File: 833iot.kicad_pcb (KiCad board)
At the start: 2 copper layers, 26.5 x 42 mm, 24 parts, among them J1 U254-051T-4BH83-F1S, J2 Conn_01x04, J3 Conn_01x02, J4 Conn_01x15_Male, J5 Conn_01x15_Male, Q1 AO3407, Q2 AO3407, SW1 SW_SPST, U1 E73-2G4M08S1E, U2 AP2112K-3.3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

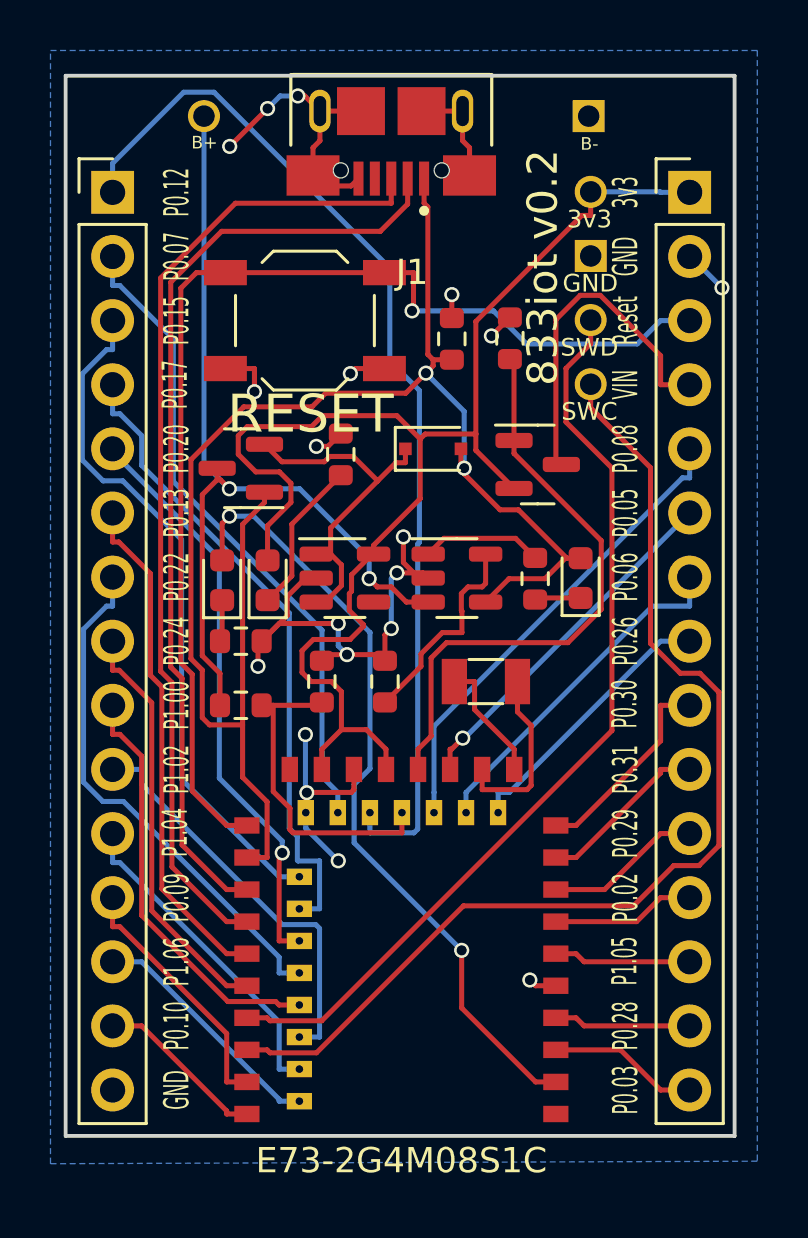
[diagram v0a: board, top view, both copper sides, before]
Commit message: fix vias issue
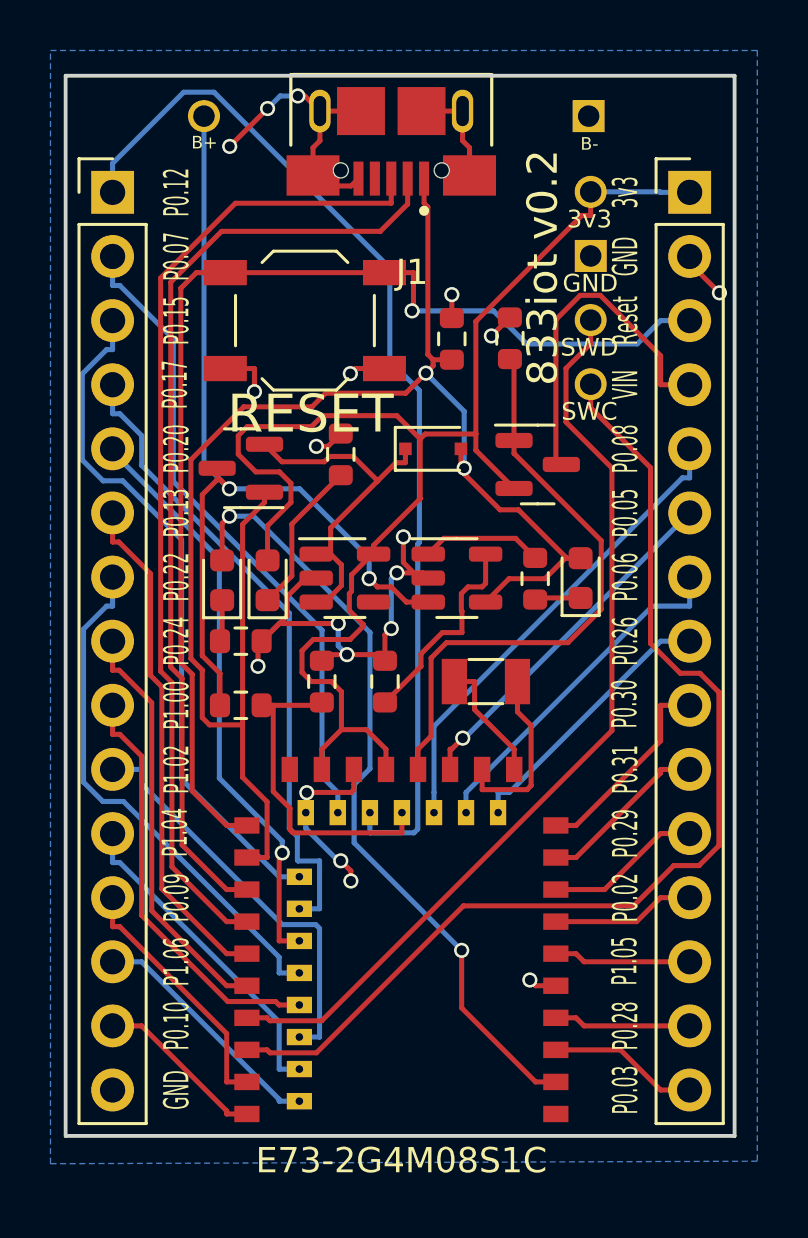
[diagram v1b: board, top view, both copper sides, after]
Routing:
- net GND: track 53.6 -> 52.5 mm
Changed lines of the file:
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@@
   (segment (start 28.4025 23.0028) (end 29.6528 23.0028) (width 0.2) (layer "F.Cu") (net 2))
   (segment (start 24.6953 36.285) (end 25.2025 35.7778) (width 0.2) (layer "F.Cu") (net 2))
+  (segment (start 39.0225 28.7628) (end 39.0225 29.022742) (width 0.2) (layer "F.Cu") (net 2))
   (segment (start 22.767525 43.302775) (end 25.102533 43.302775) (width 0.2) (layer "F.Cu") (net 2))
   (segment (start 24.1025 25.5528) (end 24.1025 24.4525) (width 0.2) (layer "F.Cu") (net 2))
@@
   (segment (start 23.0787 42.9916) (end 23.0787 42.2345) (width 0.2) (layer "F.Cu") (net 2))
   (segment (start 23.0787 42.2345) (end 23.8104 41.5028) (width 0.2) (layer "F.Cu") (net 2))
+  (segment (start 25.602533 53.102775) (end 25.202533 52.702775) (width 0.2) (layer "F.Cu") (net 2))
   (segment (start 25.6121 49.9945) (end 25.7225 49.8841) (width 0.2) (layer "F.Cu") (net 2))
   (segment (start 27.426013 41.29753) (end 28.45973 41.29753) (width 0.2) (layer "F.Cu") (net 2))
   (segment (start 22.0675 44.0028) (end 22.767525 43.302775) (width 0.2) (layer "F.Cu") (net 2))
+  (segment (start 25.602533 53.502775) (end 25.602533 53.102775) (width 0.2) (layer "F.Cu") (net 2))
   (segment (start 23.8155 50.7948) (end 23.8155 49.9945) (width 0.2) (layer "F.Cu") (net 2))
   (segment (start 28.2988 41.5028) (end 28.665 41.5028) (width 0.2) (layer "F.Cu") (net 2))
@@
   (segment (start 24.3775 24.1775) (end 24.1025 24.4525) (width 0.2) (layer "F.Cu") (net 2))
   (segment (start 26.9525 44.7778) (end 26.9525 43.752808) (width 0.2) (layer "F.Cu") (net 2))
+  (segment (start 39.0225 29.022742) (end 40.202533 30.202775) (width 0.2) (layer "F.Cu") (net 2))
   (segment (start 33.7215 57.6528) (end 32.9212 57.6528) (width 0.2) (layer "F.Cu") (net 2))
   (segment (start 26.0025 23.0028) (end 24.7522 23.0028) (width 0.2) (layer "F.Cu") (net 2))
@@
   (via (at 25.102533 43.302775) (size 0.6) (drill 0.4) (layers "F.Cu" "B.Cu") (net 2))
   (via (at 21.9229 44.9964) (size 0.6) (drill 0.4) (layers "F.Cu" "B.Cu") (net 2))
-  (via (at 40.302533 30.002775) (size 0.6) (drill 0.4) (layers "F.Cu" "B.Cu") (net 2))
+  (via (at 25.602533 53.502775) (size 0.6) (drill 0.4) (layers "F.Cu" "B.Cu") (free) (net 2))
   (via (at 22.302533 22.902775) (size 0.6) (drill 0.4) (layers "F.Cu" "B.Cu") (net 2))
   (via (at 23.856657 50.003498) (size 0.6) (drill 0.4) (layers "F.Cu" "B.Cu") (net 2))
   (via (at 20.802533 24.402775) (size 0.6) (drill 0.4) (layers "F.Cu" "B.Cu") (net 2))
   (via (at 27.6826 39.871) (size 0.6) (drill 0.4) (layers "F.Cu" "B.Cu") (net 2))
+  (via (at 25.202533 52.702775) (size 0.6) (drill 0.4) (layers "F.Cu" "B.Cu") (free) (net 2))
   (via (at 32.6929 57.4245) (size 0.6) (drill 0.4) (layers "F.Cu" "B.Cu") (net 2))
   (via (at 27.426013 41.29753) (size 0.6) (drill 0.4) (layers "F.Cu" "B.Cu") (net 2))
+  (via (at 40.202533 30.202775) (size 0.6) (drill 0.4) (layers "F.Cu" "B.Cu") (free) (net 2))
   (via (at 21.7828 34.1195) (size 0.6) (drill 0.4) (layers "F.Cu" "B.Cu") (net 2))
   (via (at 29.6025 30.2728) (size 0.6) (drill 0.4) (layers "F.Cu" "B.Cu") (net 2))
-  (via (at 25.102533 52.702775) (size 0.6) (drill 0.4) (layers "F.Cu" "B.Cu") (net 2))
   (via (at 27.202533 43.502775) (size 0.6) (drill 0.4) (layers "F.Cu" "B.Cu") (net 2))
-  (via (at 23.802533 47.702775) (size 0.6) (drill 0.4) (layers "F.Cu" "B.Cu") (free) (net 2))
   (via (at 31.1692 31.9111) (size 0.6) (drill 0.4) (layers "F.Cu" "B.Cu") (net 2))
   (via (at 24.2364 36.285) (size 0.6) (drill 0.4) (layers "F.Cu" "B.Cu") (net 2))
@@
   (segment (start 23.502533 22.402775) (end 22.802533 22.402775) (width 0.2) (layer "B.Cu") (net 2))
   (segment (start 27.202533 43.502775) (end 27.202533 41.52101) (width 0.2) (layer "B.Cu") (net 2))
+  (segment (start 25.102533 52.702775) (end 25.202533 52.702775) (width 0.2) (layer "B.Cu") (net 2))
   (segment (start 25.102533 44.188933) (end 25.4486 44.535) (width 0.2) (layer "B.Cu") (net 2))
   (segment (start 22.802533 22.402775) (end 22.302533 22.902775) (width 0.2) (layer "B.Cu") (net 2))
-  (segment (start 23.802533 49.949374) (end 23.856657 50.003498) (width 0.2) (layer "B.Cu") (net 2))
-  (segment (start 39.062558 28.7628) (end 40.302533 30.002775) (width 0.2) (layer "B.Cu") (net 2))
-  (segment (start 23.802533 47.702775) (end 23.802533 49.949374) (width 0.2) (layer "B.Cu") (net 2))
   (segment (start 39.0225 28.7628) (end 39.062558 28.7628) (width 0.2) (layer "B.Cu") (net 2))
   (segment (start 32.965 42.2903) (end 32.9025 42.3528) (width 0.2) (layer "F.Cu") (net 3))
